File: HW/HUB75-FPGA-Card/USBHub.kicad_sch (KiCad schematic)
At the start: 12 parts, among them J10 USB_A_Stacked, J9 USB_C_Receptacle_USB2.0, U12 USBLC6-2SC6, U13 CH334R, Y1 Crystal_GND24

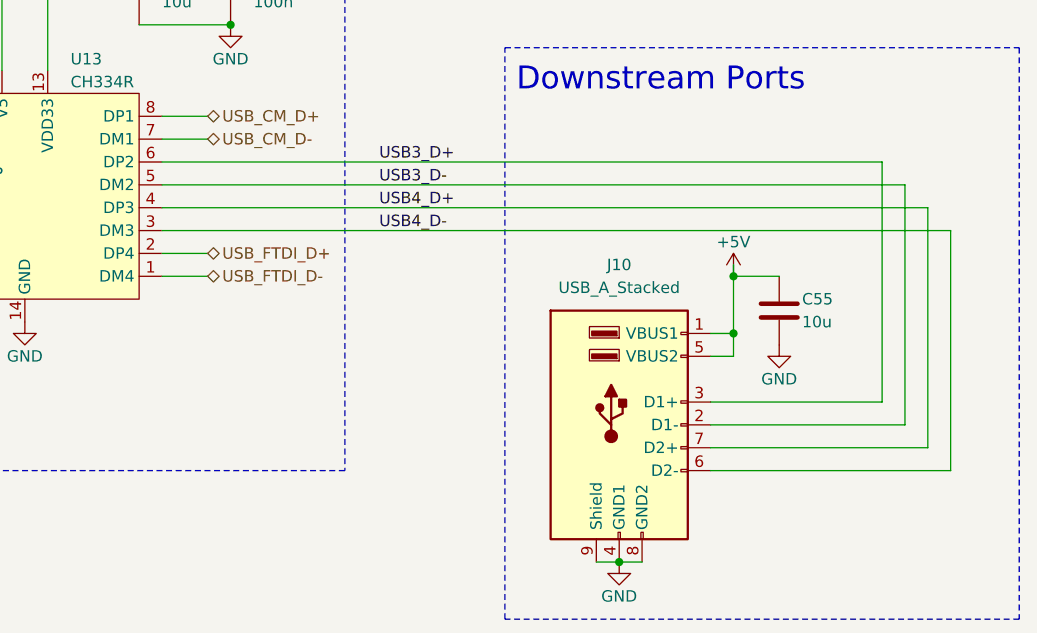
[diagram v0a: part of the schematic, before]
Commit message: finalize pcb and generate production files for first run
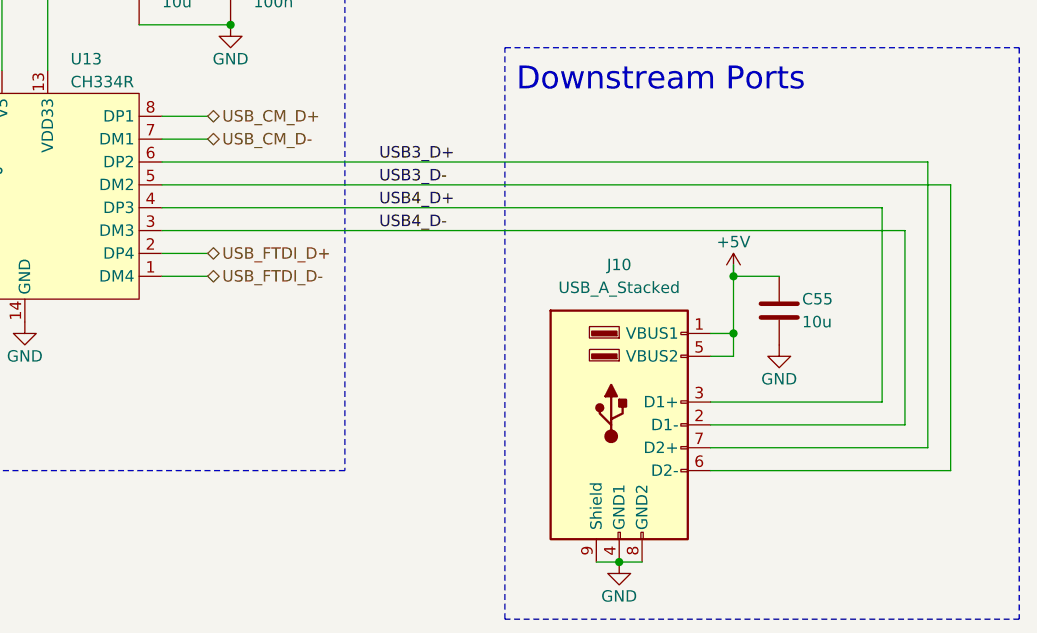
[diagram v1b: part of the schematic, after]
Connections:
- net USB3_D+: now also J10.7 (D2+); no longer J10.3 (D1+)
- net USB3_D-: now also J10.6 (D2-); no longer J10.2 (D1-)
- net USB4_D+: now also J10.3 (D1+); no longer J10.7 (D2+)
- net USB4_D-: now also J10.2 (D1-); no longer J10.6 (D2-)
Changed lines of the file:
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@@
   )
   (no_connect (at 152.4 86.36))
-  (wire (pts (xy 265.43 87.63) (xy 265.43 114.3))
-    (stroke (width 0) (type default))
-  )
   (wire (pts (xy 246.38 104.14) (xy 243.84 104.14))
     (stroke (width 0) (type default))
@@
     (stroke (width 0) (type default))
   )
-  (wire (pts (xy 267.97 90.17) (xy 267.97 116.84))
-    (stroke (width 0) (type default))
-  )
   (wire (pts (xy 170.18 74.93) (xy 170.18 62.23))
     (stroke (width 0) (type default))
@@
     (stroke (width 0) (type default))
   )
+  (wire (pts (xy 270.51 87.63) (xy 270.51 119.38))
+    (stroke (width 0) (type default))
+  )
   (wire (pts (xy 67.31 71.12) (xy 67.31 73.66))
     (stroke (width 0) (type default))
@@
     (stroke (width 0) (type default))
   )
+  (wire (pts (xy 262.89 90.17) (xy 262.89 111.76))
+    (stroke (width 0) (type default))
+  )
   (wire (pts (xy 262.89 111.76) (xy 243.84 111.76))
     (stroke (width 0) (type default))
@@
     (stroke (width 0) (type default))
   )
-  (wire (pts (xy 182.88 92.71) (xy 270.51 92.71))
+  (wire (pts (xy 182.88 92.71) (xy 265.43 92.71))
     (stroke (width 0) (type default))
   )
@@
     (stroke (width 0) (type default))
   )
-  (wire (pts (xy 270.51 92.71) (xy 270.51 119.38))
-    (stroke (width 0) (type default))
-  )
   (wire (pts (xy 182.88 82.55) (xy 187.96 82.55))
     (stroke (width 0) (type default))
@@
     (stroke (width 0) (type default))
   )
-  (wire (pts (xy 182.88 90.17) (xy 267.97 90.17))
+  (wire (pts (xy 182.88 90.17) (xy 262.89 90.17))
     (stroke (width 0) (type default))
   )
@@
     (stroke (width 0) (type default))
   )
+  (wire (pts (xy 265.43 92.71) (xy 265.43 114.3))
+    (stroke (width 0) (type default))
+  )
   (wire (pts (xy 133.35 92.71) (xy 152.4 92.71))
     (stroke (width 0) (type default))
@@
     (stroke (width 0) (type default))
   )
-  (wire (pts (xy 262.89 85.09) (xy 262.89 111.76))
-    (stroke (width 0) (type default))
-  )
   (wire (pts (xy 100.33 73.66) (xy 100.33 71.12))
     (stroke (width 0) (type default))
   )
+  (wire (pts (xy 267.97 85.09) (xy 267.97 116.84))
+    (stroke (width 0) (type default))
+  )
   (wire (pts (xy 139.7 95.25) (xy 130.81 95.25))
     (stroke (width 0) (type default))
@@
     (stroke (width 0) (type default))
   )
-  (wire (pts (xy 182.88 85.09) (xy 262.89 85.09))
+  (wire (pts (xy 182.88 85.09) (xy 267.97 85.09))
     (stroke (width 0) (type default))
   )
@@
     (stroke (width 0) (type default))
   )
-  (wire (pts (xy 182.88 87.63) (xy 265.43 87.63))
+  (wire (pts (xy 182.88 87.63) (xy 270.51 87.63))
     (stroke (width 0) (type default))
   )
@@
     (instances
       (project "HUB75-FPGA-Card"
-        (path "/12c1dc17-a9d4-409d-a42e-fc131eeff0fd/45acbd2b-2398-4f26-b8e7-9bd133bc66a8"
+        (path "/12c1dc17-a9d4-409d-a42e-fc131eeff0fd/fd3ee05a-2565-4215-8abb-7122eb6c53a0"
           (reference "Y1") (unit 1)
-        )
-        (path "/12c1dc17-a9d4-409d-a42e-fc131eeff0fd/fd3ee05a-2565-4215-8abb-7122eb6c53a0"
-          (reference "Y1") (unit 1)

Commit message: saving hardware progress
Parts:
- removed J10: USB_A_Stacked, Connector_USB:USB_A_CUI_UJ2-ADH-TH_Horizontal_Stacked, symbol Connector:USB_A_Stacked
- removed J9: USB_C_Receptacle_USB2.0, Connector_USB:USB_C_Receptacle_GCT_USB4105-xx-A_16P_TopMnt_Horizontal, symbol Connector:USB_C_Receptacle_USB2.0
- added J8: USB_A, Project:SS-52100-002, symbol Connector:USB_A
- added J9: USB_C_Receptacle_USB2.0_14P, Project:GCT_USB4145-03-0170-C_REVA2, symbol Connector:USB_C_Receptacle_USB2.0_14P
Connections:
- net USB4_D+ is gone; now on net USB_CM_D+: U13.4 (DP3)
- net USB4_D- is gone; now on net USB_CM_D-: U13.3 (DM3)
- net +5V: now also J8.1 (VBUS), J9.A4 (VBUS), J9.A9 (VBUS), J9.B4 (VBUS), J9.B9 (VBUS)
- net GND: now also J8.4 (GND), J8.5 (Shield), J9.A1 (GND), J9.A12 (GND), J9.B1 (GND), J9.B12 (GND), J9.S1 (SHIELD)
- net RAW_D+: now also U12.4 (I/O2), J9.A6 (D+), J9.B6 (D+); no longer U12.6 (I/O1)
- net RAW_D-: now also U12.6 (I/O1), J9.A7 (D-), J9.B7 (D-); no longer U12.4 (I/O2)
- net USBU_D+: now also U12.3 (I/O2); no longer U12.1 (I/O1)
- net USBU_D-: now also U12.1 (I/O1); no longer U12.3 (I/O2)
- net USB_CM_D+: no longer U13.8 (DP1)
- net USB_CM_D-: no longer U13.7 (DM1)
- net at R20.1: now also J9.A5 (CC1)
- net at R21.1: now also J9.B5 (CC2)
- net USB3_D+ renamed USB_MCU_D+
- net USB3_D- renamed USB_MCU_D-
- new net USB_EXT_D+: J8.3 (D+), U13.8 (DP1)
- new net USB_EXT_D-: J8.2 (D-), U13.7 (DM1)
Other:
- note added: "Downstream Port"
- note removed: "Downstream Ports"

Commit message: initial v1.1 board layout
still needs rp2040 pins routed
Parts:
- renumbered C54 to C45, C51 to C46, C52 to C47, C53 to C48, C55 to C49, J9 to J10, J8 to J11, U12 to U11, U13 to U12
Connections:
- net USB_CM_D+: now also U12.6 (DP2); no longer U12.4 (DP3)
- net USB_CM_D-: now also U12.5 (DM2); no longer U12.3 (DM3)
- net USB_FTDI_D+: now also U12.4 (DP3); no longer U12.2 (DP4)
- net USB_FTDI_D-: now also U12.3 (DM3); no longer U12.1 (DM4)
- net USB_MCU_D+: now also U12.2 (DP4); no longer U12.6 (DP2)
- net USB_MCU_D-: now also U12.1 (DM4); no longer U12.5 (DM2)

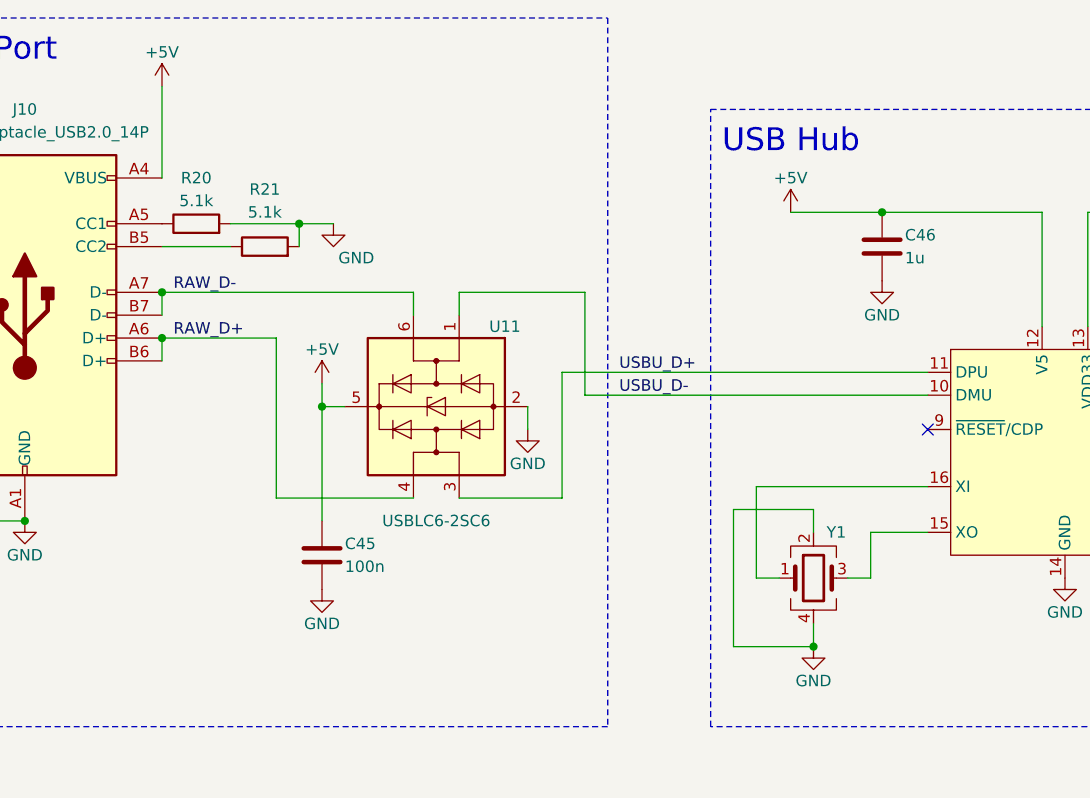
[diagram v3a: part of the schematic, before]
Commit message: migrate to kicad 8
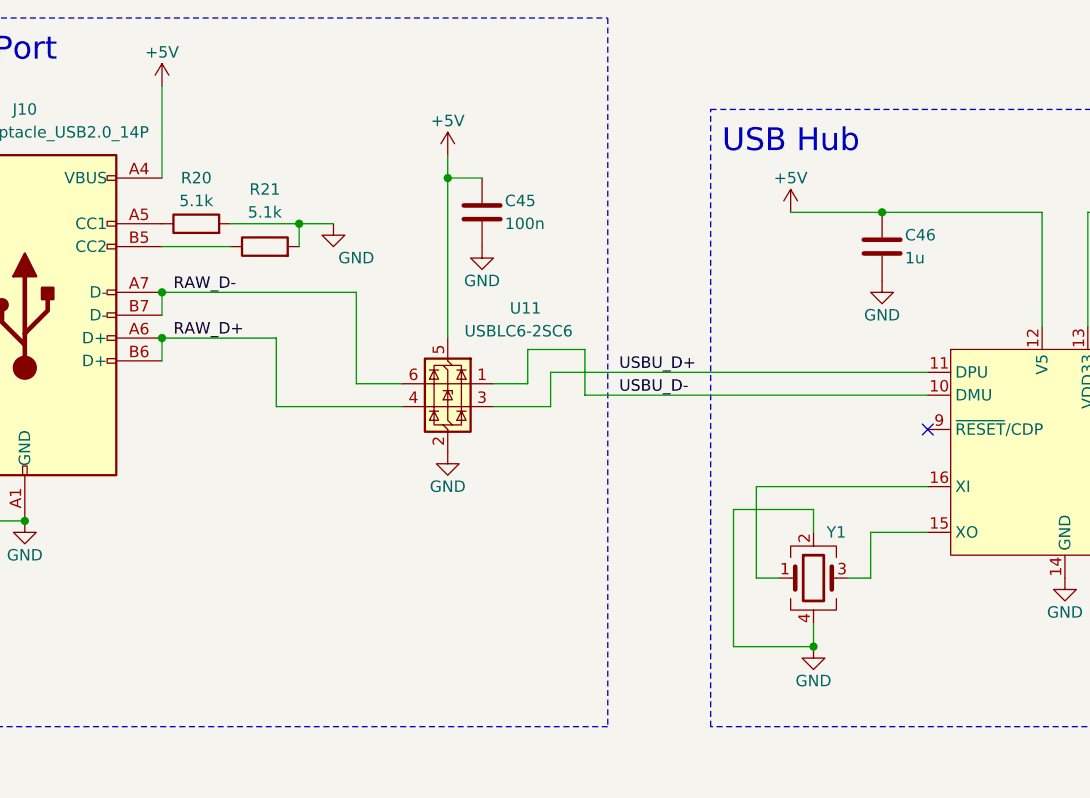
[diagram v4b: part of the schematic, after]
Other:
- moved on the sheet: C45
